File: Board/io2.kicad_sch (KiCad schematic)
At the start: 25 parts, among them J1 DIN-6, J14 Extended_PET_keyboard_connect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, J2 Conn_01x23, P2 IEEE488FLATCABLE, U1 XC6SLX9-TQG144, U10 74LS06, U11 SN74LVC245APW, U12 4051, U13 4051, U14 74LVC1G04, U4 SN75160BDW, U5 SN75161BDW, U6 LSF0204Q, U7 LSF0204Q, U8 LSF0204Q, U9 LSF0204Q

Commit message: start working on 1.0b
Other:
- note added: "CSA-CBMIO-V1.0B"
- note added: "Note: - FPGA has do to internal pull-ups - 7516x are LS type which should have internal pull-ups. Optional external pull ups can be used - ATNA handling is still missing, need two more I/O pins for Serial and Parallel... (or sacrifice two from userport...)"
- note removed: "CSA-CBMIO-V1.0A"
- note removed: "Note: - FPGA has do to internal pull-ups - 7516x are LS type which should have internal pull-ups. Optional external pull ups can be used"
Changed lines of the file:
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@@
 		)
 	)
-	(text "CSA-CBMIO-V1.0A"
+	(text "CSA-CBMIO-V1.0B"
 		(exclude_from_sim no)
 		(at 339.09 261.112 0)
@@
 		)
 	)
-	(text "Note:\n- FPGA has do to internal pull-ups\n- 7516x are LS type which should have internal\n  pull-ups. Optional external pull ups can be used"
+	(text "Note:\n- FPGA has do to internal pull-ups\n- 7516x are LS type which should have internal\n  pull-ups. Optional external pull ups can be used\n- ATNA handling is still missing, need two\n  more I/O pins for Serial and Parallel...\n  (or sacrifice two from userport...)"
 		(exclude_from_sim no)
-		(at 320.802 28.956 0)
+		(at 207.518 231.14 0)
 		(effects
 			(font
-				(size 1.27 1.27)
+				(size 2 2)
 			)
 			(justify left)

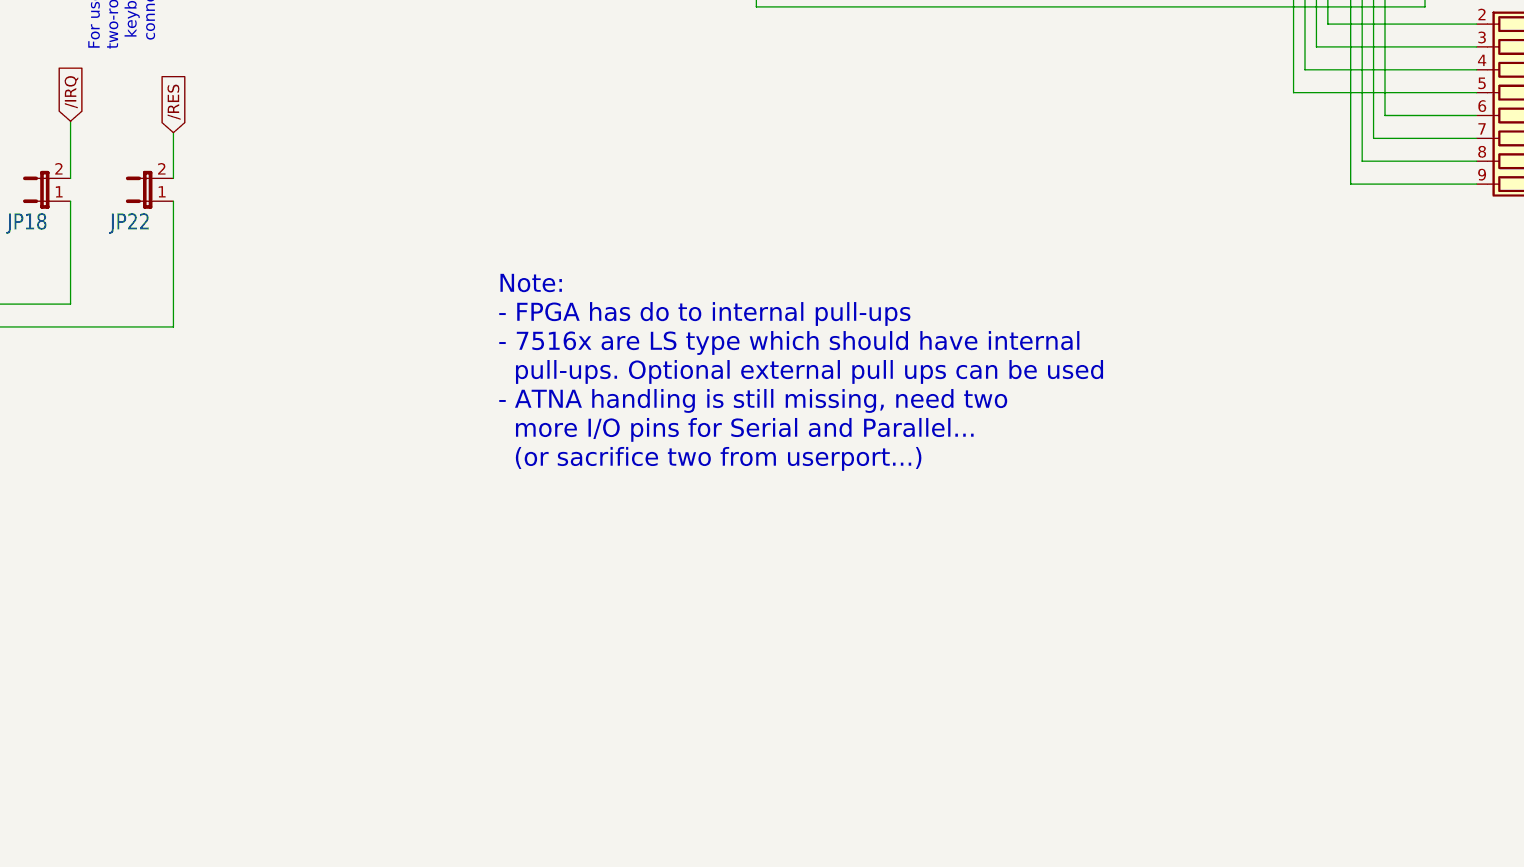
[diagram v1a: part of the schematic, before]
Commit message: added comments and TODOs on schem
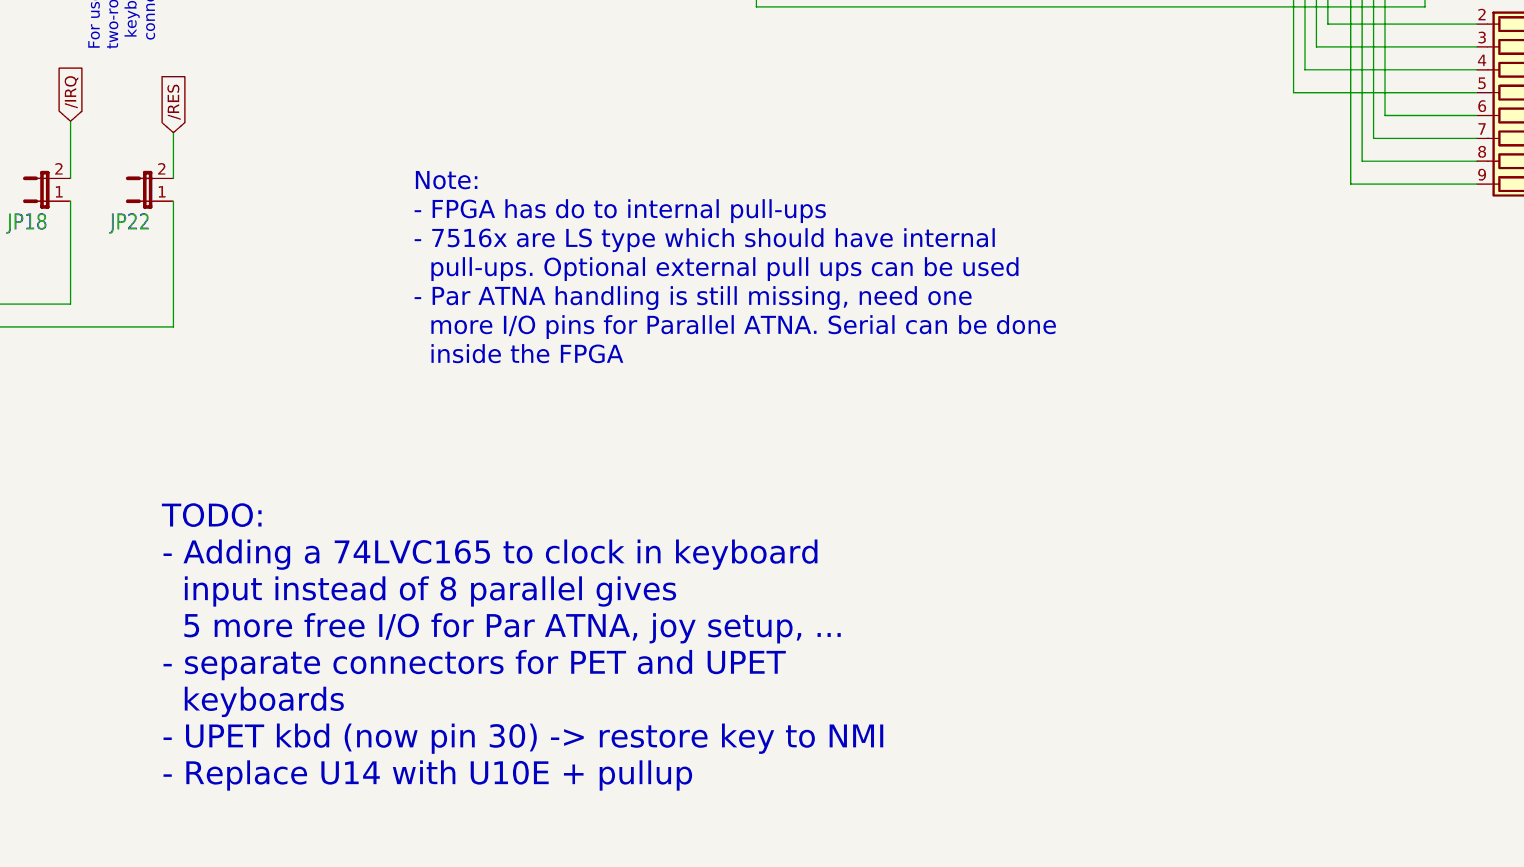
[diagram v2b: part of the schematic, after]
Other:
- note added: "Note: - FPGA has do to internal pull-ups - 7516x are LS type which should have internal pull-ups. Optional external pull ups can be used - Par ATNA handling is still missing, need one more I/O pins for Parallel ATNA. Serial can be done inside the FPGA"
- note added: "TODO: - Adding a 74LVC165 to clock in keyboard input instead of 8 parallel gives 5 more free I/O for Par ATNA, joy setup, ... - separate connectors for PET and UPET keyboards - UPET kbd (now pin 30) -> restore key to NMI - Replace U14 with U10E + pullup"
- note removed: "Note: - FPGA has do to internal pull-ups - 7516x are LS type which should have internal pull-ups. Optional external pull ups can be used - ATNA handling is still missing, need two more I/O pins for Serial and Parallel... (or sacrifice two from userport...)"
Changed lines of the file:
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@@
 		)
 	)
-	(text "Note:\n- FPGA has do to internal pull-ups\n- 7516x are LS type which should have internal\n  pull-ups. Optional external pull ups can be used\n- ATNA handling is still missing, need two\n  more I/O pins for Serial and Parallel...\n  (or sacrifice two from userport...)"
+	(text "Note:\n- FPGA has do to internal pull-ups\n- 7516x are LS type which should have internal\n  pull-ups. Optional external pull ups can be used\n- Par ATNA handling is still missing, need one\n  more I/O pins for Parallel ATNA. Serial can be done\n  inside the FPGA"
 		(exclude_from_sim no)
-		(at 207.518 231.14 0)
+		(at 198.12 219.71 0)
 		(effects
 			(font
@@
 		)
 	)
+	(text "TODO:\n- Adding a 74LVC165 to clock in keyboard\n  input instead of 8 parallel gives\n  5 more free I/O for Par ATNA, joy setup, ...\n- separate connectors for PET and UPET\n  keyboards\n- UPET kbd (now pin 30) -> restore key to NMI\n- Replace U14 with U10E + pullup"
+		(exclude_from_sim no)
+		(at 170.18 261.62 0)
+		(effects
+			(font
+				(size 2.54 2.54)
+			)
+			(justify left)
+		)
+	)
 	(junction
 		(at 392.43 120.65)
@@
 		)
 		(instances
-			(project ""
+			(project "csa_petio_v1"
 				(path "/e52c695d-6540-4a56-9880-06c7d9f215a5/70ccb61c-5015-4d74-a36e-b1514308c68b"
 					(reference "J2")
@@
 		)
 		(instances
-			(project ""
+			(project "csa_petio_v1"
 				(path "/e52c695d-6540-4a56-9880-06c7d9f215a5/70ccb61c-5015-4d74-a36e-b1514308c68b"
 					(reference "U10")
@@
 		)
 		(instances
-			(project ""
+			(project "csa_petio_v1"
 				(path "/e52c695d-6540-4a56-9880-06c7d9f215a5/70ccb61c-5015-4d74-a36e-b1514308c68b"
 					(reference "U10")
@@
 		)
 		(instances
-			(project ""
+			(project "csa_petio_v1"
 				(path "/e52c695d-6540-4a56-9880-06c7d9f215a5/70ccb61c-5015-4d74-a36e-b1514308c68b"
 					(reference "U12")
@@
 		)
 		(instances
-			(project ""
+			(project "csa_petio_v1"
 				(path "/e52c695d-6540-4a56-9880-06c7d9f215a5/70ccb61c-5015-4d74-a36e-b1514308c68b"
 					(reference "RN6")
@@
 		)
 		(instances
-			(project ""
+			(project "csa_petio_v1"
 				(path "/e52c695d-6540-4a56-9880-06c7d9f215a5/70ccb61c-5015-4d74-a36e-b1514308c68b"
 					(reference "RN1")
@@
 		)
 		(instances
-			(project ""
+			(project "csa_petio_v1"
 				(path "/e52c695d-6540-4a56-9880-06c7d9f215a5/70ccb61c-5015-4d74-a36e-b1514308c68b"
 					(reference "U10")
@@
 		)
 		(instances
-			(project ""
+			(project "csa_petio_v1"
 				(path "/e52c695d-6540-4a56-9880-06c7d9f215a5/70ccb61c-5015-4d74-a36e-b1514308c68b"
 					(reference "U14")
@@
 		)
 		(instances
-			(project ""
+			(project "csa_petio_v1"
 				(path "/e52c695d-6540-4a56-9880-06c7d9f215a5/70ccb61c-5015-4d74-a36e-b1514308c68b"
 					(reference "U10")
@@
 		)
 		(instances
-			(project ""
+			(project "csa_petio_v1"
 				(path "/e52c695d-6540-4a56-9880-06c7d9f215a5/70ccb61c-5015-4d74-a36e-b1514308c68b"
 					(reference "J1")
@@
 		)
 		(instances
-			(project ""
+			(project "csa_petio_v1"
 				(path "/e52c695d-6540-4a56-9880-06c7d9f215a5/70ccb61c-5015-4d74-a36e-b1514308c68b"
 					(reference "U10")
@@
 		)
 		(instances
-			(project ""
+			(project "csa_petio_v1"
 				(path "/e52c695d-6540-4a56-9880-06c7d9f215a5/70ccb61c-5015-4d74-a36e-b1514308c68b"
 					(reference "U10")

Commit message: note for ATNA
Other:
- note added: "Note: - FPGA has do to internal pull-ups - Par ATNA handling is still missing, need one more I/O pins for Parallel ATNA. Serial can be done inside the FPGA"
- note removed: "Note: - FPGA has do to internal pull-ups - 7516x are LS type which should have internal pull-ups. Optional external pull ups can be used - Par ATNA handling is still missing, need one more I/O pins for Parallel ATNA. Serial can be done inside the FPGA"
- moved on the sheet: U10G
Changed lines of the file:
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@@
 		)
 	)
-	(text "Note:\n- FPGA has do to internal pull-ups\n- 7516x are LS type which should have internal\n  pull-ups. Optional external pull ups can be used\n- Par ATNA handling is still missing, need one\n  more I/O pins for Parallel ATNA. Serial can be done\n  inside the FPGA"
+	(text "Note:\n- FPGA has do to internal pull-ups\n- Par ATNA handling is still missing, need one\n  more I/O pins for Parallel ATNA. Serial can be done\n  inside the FPGA"
 		(exclude_from_sim no)
-		(at 198.12 219.71 0)
+		(at 205.74 213.36 0)
 		(effects
 			(font
@@
 	(wire
 		(pts
-			(xy 218.44 27.94) (xy 218.44 30.48)
+			(xy 191.77 27.94) (xy 191.77 30.48)
 		)
 		(stroke
@@
 	(wire
 		(pts
-			(xy 218.44 57.15) (xy 218.44 55.88)
+			(xy 191.77 57.15) (xy 191.77 55.88)
 		)
 		(stroke
@@
 	(symbol
 		(lib_id "cbm_ultipet_v1-eagle-import:GND")
-		(at 218.44 59.69 0)
+		(at 191.77 59.69 0)
 		(unit 1)
 		(exclude_from_sim no)
@@
 		(dnp no)
 		(property "Reference" "#GND025"
-			(at 218.44 59.69 0)
+			(at 191.77 59.69 0)
 			(effects
 				(font
@@
 		)
 		(property "Value" "GND"
-			(at 215.9 62.23 0)
+			(at 189.23 62.23 0)
 			(effects
 				(font
@@
 		)
 		(property "Footprint" ""
-			(at 218.44 59.69 0)
+			(at 191.77 59.69 0)
 			(effects
 				(font
@@
 		)
 		(property "Datasheet" ""
-			(at 218.44 59.69 0)
+			(at 191.77 59.69 0)
 			(effects
 				(font
@@
 		)
 		(property "Description" ""
-			(at 218.44 59.69 0)
+			(at 191.77 59.69 0)
 			(effects
 				(font
@@
 	(symbol
 		(lib_id "csa_petio_v1-eagle-import:VCC")
-		(at 218.44 25.4 0)
+		(at 191.77 25.4 0)
 		(unit 1)
 		(exclude_from_sim no)
@@
 		(dnp no)
 		(property "Reference" "#V07"
-			(at 218.44 25.4 0)
+			(at 191.77 25.4 0)
 			(effects
 				(font
@@
 		)
 		(property "Value" "VCC"
-			(at 216.535 22.225 0)
+			(at 189.865 22.225 0)
 			(effects
 				(font
@@
 		)
 		(property "Footprint" ""
-			(at 218.44 25.4 0)
+			(at 191.77 25.4 0)
 			(effects
 				(font
@@
 		)
 		(property "Datasheet" ""
-			(at 218.44 25.4 0)
+			(at 191.77 25.4 0)
 			(effects
 				(font
@@
 		)
 		(property "Description" ""
-			(at 218.44 25.4 0)
+			(at 191.77 25.4 0)
 			(effects
 				(font
@@
 	(symbol
 		(lib_id "74xx:74LS06")
-		(at 218.44 43.18 0)
+		(at 191.77 43.18 0)
 		(unit 7)
 		(exclude_from_sim no)
@@
 		(fields_autoplaced yes)
 		(property "Reference" "U10"
-			(at 224.79 41.9099 0)
+			(at 198.12 41.9099 0)
 			(effects
 				(font
@@
 		)
 		(property "Value" "74LS06"
-			(at 224.79 44.4499 0)
+			(at 198.12 44.4499 0)
 			(effects
 				(font
@@
 		)
 		(property "Footprint" "Package_SO:SO-14_3.9x8.65mm_P1.27mm"
-			(at 218.44 43.18 0)
+			(at 191.77 43.18 0)
 			(effects
 				(font
@@
 		)
 		(property "Datasheet" "http://www.ti.com/lit/gpn/sn74LS06"
-			(at 218.44 43.18 0)
+			(at 191.77 43.18 0)
 			(effects
 				(font
@@
 		)
 		(property "Description" "Inverter Open Collect"
-			(at 218.44 43.18 0)
+			(at 191.77 43.18 0)
 			(effects
 				(font
